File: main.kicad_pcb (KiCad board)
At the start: 4 copper layers, 160 x 100 mm, 287 parts, among them J1 C64AC, J2 DB50_Female, U1 OPA4202, U10 LM399, U11 OPA4202, U12 LM399, U13 LM399, U14 LM399, U15 LM399, U16 OPA4202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

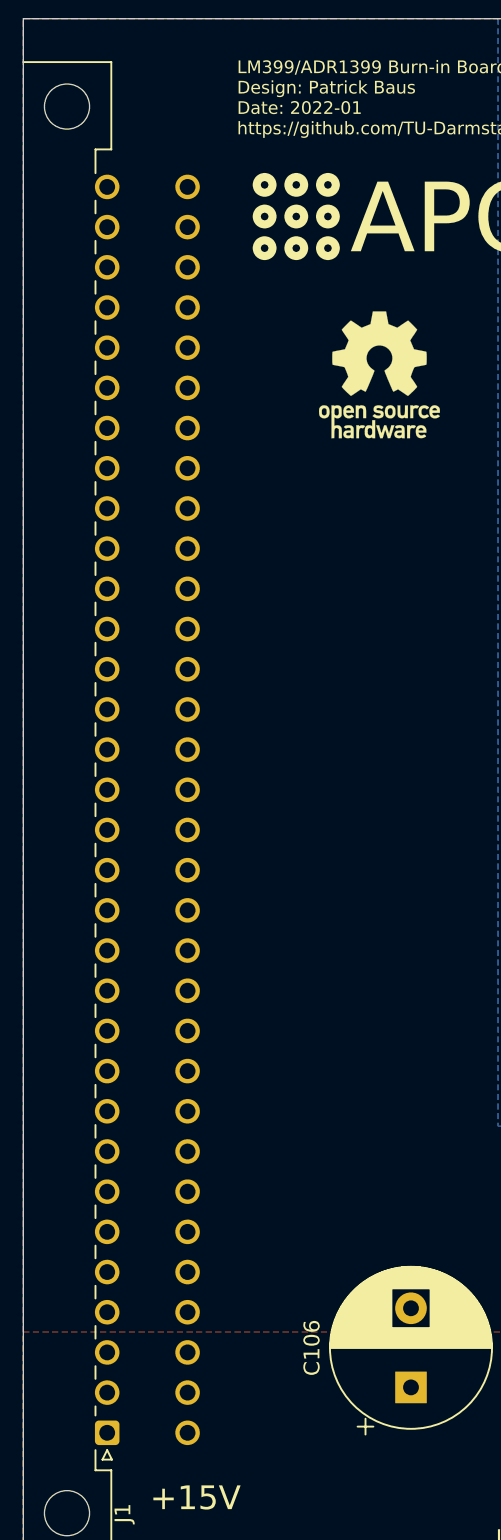
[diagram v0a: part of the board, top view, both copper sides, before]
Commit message: Fixed PCB date
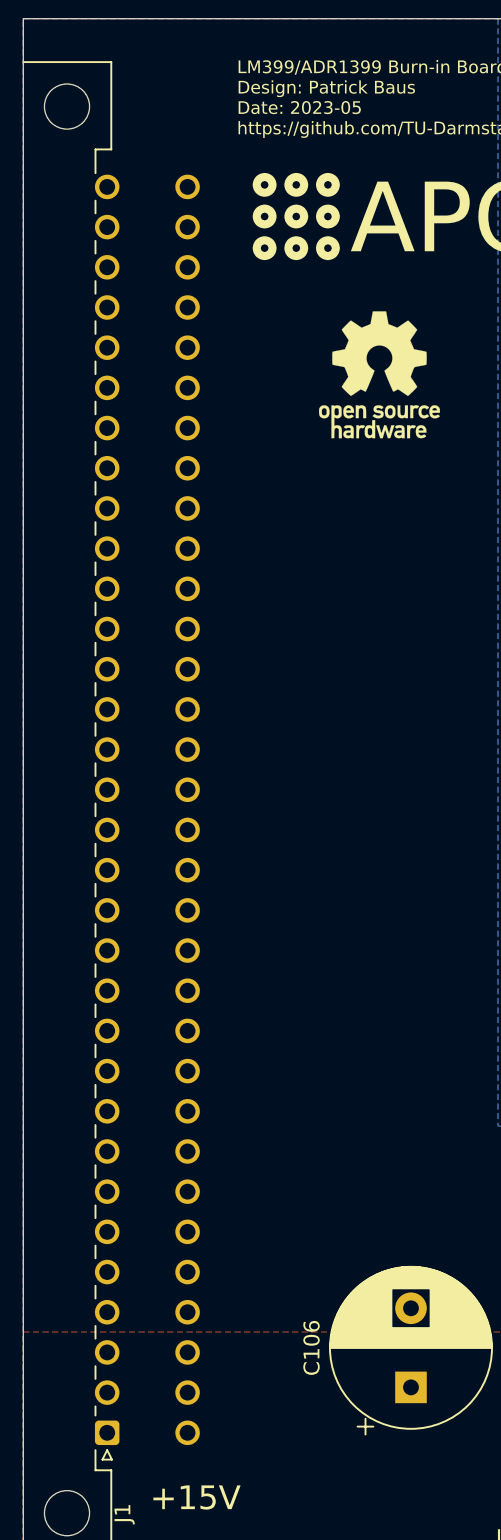
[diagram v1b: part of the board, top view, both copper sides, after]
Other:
- board text added: "LM399/ADR1399 Burn-in Board v1.0.1 Design: Patrick Baus Date: 2023-05 https://github.com/TU-Darmstadt-APQ"
- board text removed: "LM399/ADR1399 Burn-in Board v1.0.1 Design: Patrick Baus Date: 2022-01 https://github.com/TU-Darmstadt-APQ"
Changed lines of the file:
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@@
   (title_block
     (title "LM399/ADR1399 Burnin Board")
-    (date "2021-11-17")
+    (date "2023-05-27")
     (rev "v1.0.1")
     (company "TU Darmstadt, IAP, APQ")
@@
     (pad "" np_thru_hole circle (at -5.08 -2.54 90) (size 2.85 2.85) (drill 2.85) (layers "*.Cu" "*.Mask"))
     (pad "" np_thru_hole circle (at 83.82 -2.54 90) (size 2.85 2.85) (drill 2.85) (layers "*.Cu" "*.Mask"))
-    (pad "a1" thru_hole roundrect (at 0 0 90) (size 1.55 1.55) (drill 1) (layers "*.Cu" "*.Mask") (roundrect_rratio 0.16129)
+    (pad "a1" thru_hole roundrect (at 0 0 90) (size 1.55 1.55) (drill 1) (layers "*.Cu" "*.Mask") (roundrect_rratio 0.1612896774)
       (net 138 "Net-(#FLG0101-pwr)") (pinfunction "Pin_a1") (pintype "passive"))
     (pad "a2" thru_hole circle (at 2.54 0 90) (size 1.55 1.55) (drill 1) (layers "*.Cu" "*.Mask")
@@
     (effects (font (size 1.5 1.5) (thickness 0.3)) (justify left))
   )
-  (gr_text "LM399/ADR1399 Burn-in Board v1.0.1\nDesign: Patrick Baus\nDate: 2022-01\nhttps://github.com/TU-Darmstadt-APQ" (at 48.5 65) (layer "F.SilkS")
+  (gr_text "LM399/ADR1399 Burn-in Board v1.0.1\nDesign: Patrick Baus\nDate: 2023-05\nhttps://github.com/TU-Darmstadt-APQ" (at 48.5 65) (layer "F.SilkS")
     (effects (font (size 0.8 0.8) (thickness 0.15)) (justify left))
   )

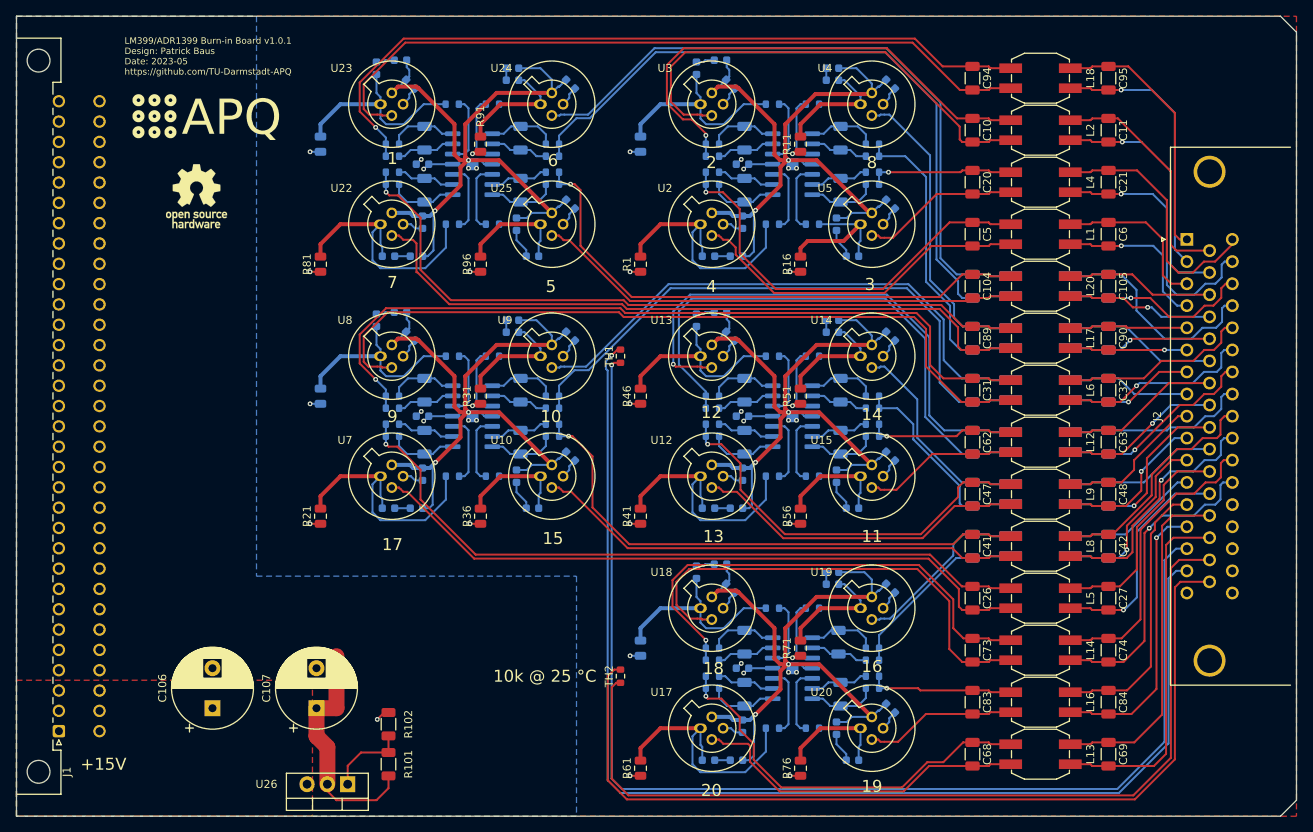
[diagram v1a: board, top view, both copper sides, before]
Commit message: Update KiCad to version 8 (#2)
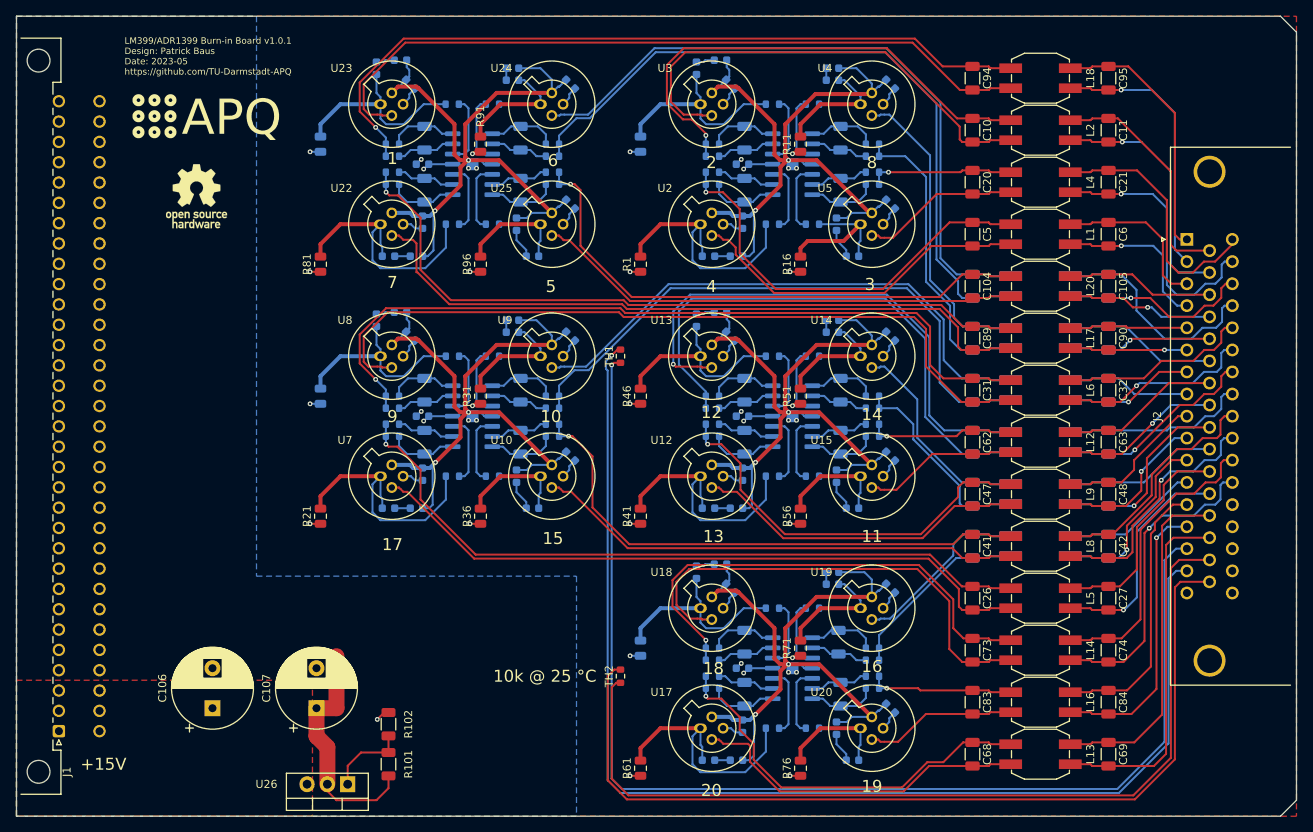
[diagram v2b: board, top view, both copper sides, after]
